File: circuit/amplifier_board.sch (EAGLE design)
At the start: 17 parts

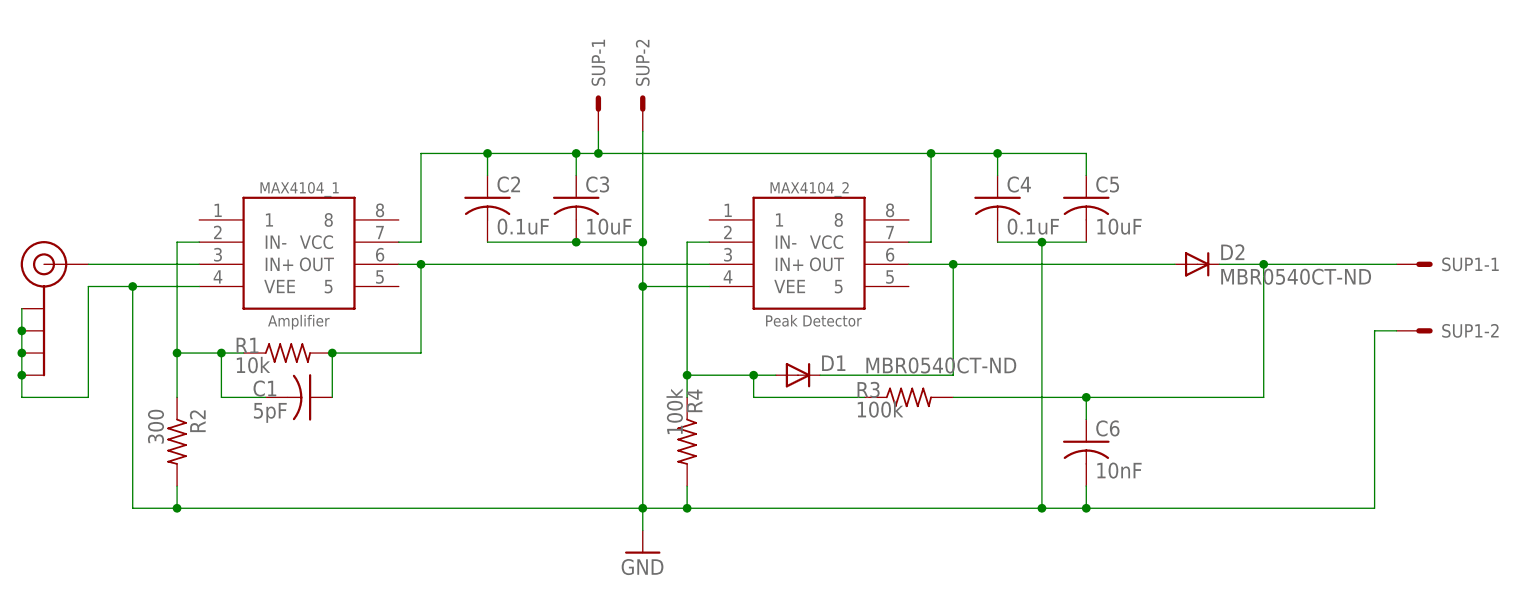
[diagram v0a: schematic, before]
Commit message: Modified board. Tried to add Spice model.
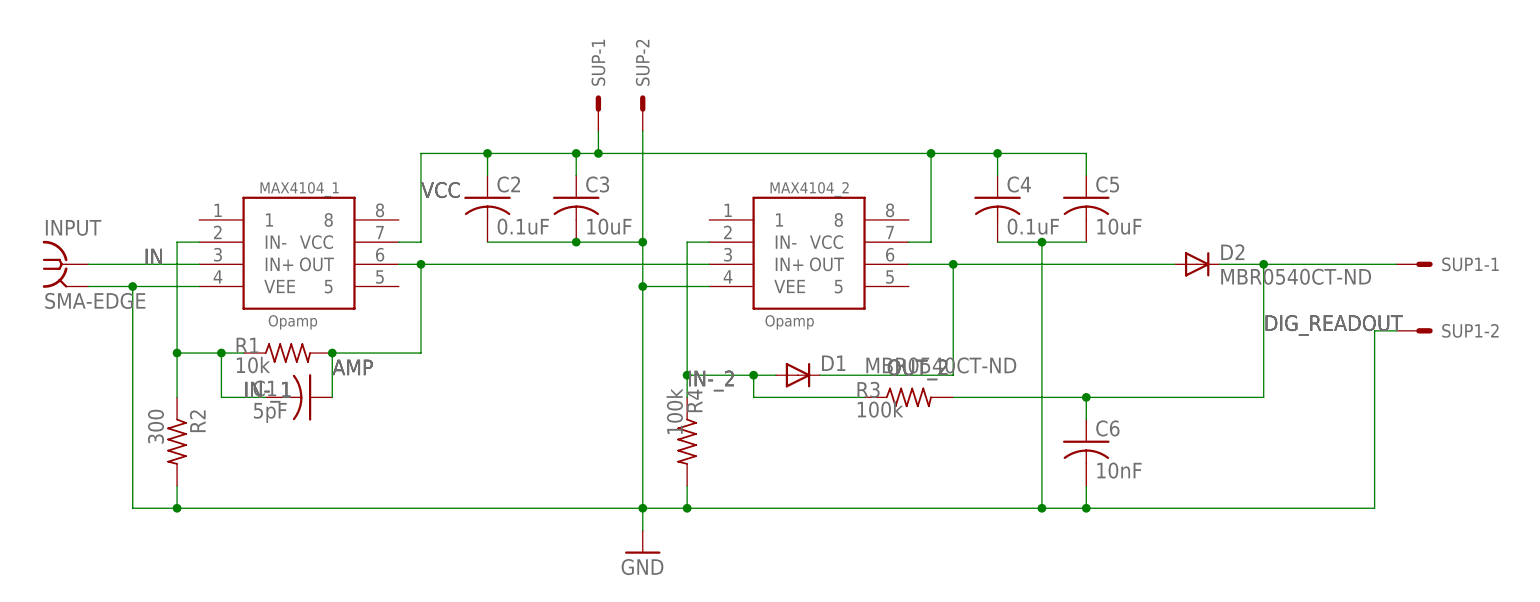
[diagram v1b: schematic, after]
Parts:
- removed IN: SMA_EDGE, SparkFun-Retired:SMA_EDGE
- added INPUT: SMA-EDGE, 000phys605parts:SMA-EDGE
- D1, D2: SPICEMODEL (none) -> DMBR0540; SPICEPREFIX (none) -> D
- MAX4104_1: value Amplifier -> Opamp; SPICEMODEL (none) -> MAX4104; SPICEPREFIX (none) -> X
- MAX4104_2: value Peak Detector -> Opamp; SPICEMODEL (none) -> MAX4104; SPICEPREFIX (none) -> X
- SUP: SPICEMODEL (none) -> VoltageSource; SPICEPREFIX (none) -> X
- SUP1: SPICEMODEL (none) -> TerminalOut; SPICEPREFIX (none) -> X
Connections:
- net GND: now also INPUT.2; no longer IN.GND@0, IN.GND@1, IN.GND@2, IN.GND@3
- net IN: now also INPUT.1; no longer IN.SIGNAL
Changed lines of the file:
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@@
 </classes>
 <parts>
-<part name="MAX4104_1" library="000phys605parts" deviceset="MAX4104" device="" value="Amplifier"/>
+<part name="MAX4104_1" library="000phys605parts" deviceset="MAX4104" device="" value="Opamp">
+<spice>
+<pinmapping isusermap="yes" isdevicewide="no">
+<pinmap gate="G$1" pin="1" pinorder="6"/>
+<pinmap gate="G$1" pin="5" pinorder="7"/>
+<pinmap gate="G$1" pin="8" pinorder="8"/>
+<pinmap gate="G$1" pin="IN+" pinorder="1"/>
+<pinmap gate="G$1" pin="IN-" pinorder="2"/>
+<pinmap gate="G$1" pin="OUT" pinorder="5"/>
+<pinmap gate="G$1" pin="VCC" pinorder="3"/>
+<pinmap gate="G$1" pin="VEE" pinorder="4"/>
+</pinmapping>
+</spice>
+<attribute name="SPICEMODEL" value="MAX4104"/>
+<attribute name="SPICEPREFIX" value="X"/>
+</part>
 <part name="R1" library="rcl" library_urn="urn:adsk.eagle:library:334" deviceset="R-US_" device="M0805" package3d_urn="urn:adsk.eagle:package:23556/1" value="10k"/>
 <part name="R2" library="rcl" library_urn="urn:adsk.eagle:library:334" deviceset="R-US_" device="M0805" package3d_urn="urn:adsk.eagle:package:23556/1" value="300"/>
@@
 <part name="C3" library="rcl" library_urn="urn:adsk.eagle:library:334" deviceset="C-US" device="C0805" package3d_urn="urn:adsk.eagle:package:23617/2" value="10uF"/>
 <part name="C2" library="rcl" library_urn="urn:adsk.eagle:library:334" deviceset="C-US" device="C0805" package3d_urn="urn:adsk.eagle:package:23617/2" value="0.1uF"/>
-<part name="SUP" library="con-garry" library_urn="urn:adsk.eagle:library:147" deviceset="332-02" device="" package3d_urn="urn:adsk.eagle:package:6810/1"/>
-<part name="MAX4104_2" library="000phys605parts" deviceset="MAX4104" device="" value="Peak Detector"/>
+<part name="SUP" library="con-garry" library_urn="urn:adsk.eagle:library:147" deviceset="332-02" device="" package3d_urn="urn:adsk.eagle:package:6810/1">
+<spice>
+<pinmapping isusermap="yes" isdevicewide="no">
+<pinmap gate="-1" pin="S" pinorder="1"/>
+<pinmap gate="-2" pin="S" pinorder="2"/>
+</pinmapping>
+</spice>
+<attribute name="SPICEMODEL" value="VoltageSource"/>
+<attribute name="SPICEPREFIX" value="X"/>
+</part>
+<part name="MAX4104_2" library="000phys605parts" deviceset="MAX4104" device="" value="Opamp">
+<spice>
+<pinmapping isusermap="yes" isdevicewide="no">
+<pinmap gate="G$1" pin="1" pinorder="6"/>
+<pinmap gate="G$1" pin="5" pinorder="7"/>
+<pinmap gate="G$1" pin="8" pinorder="8"/>
+<pinmap gate="G$1" pin="IN+" pinorder="1"/>
+<pinmap gate="G$1" pin="IN-" pinorder="2"/>
+<pinmap gate="G$1" pin="OUT" pinorder="5"/>
+<pinmap gate="G$1" pin="VCC" pinorder="3"/>
+<pinmap gate="G$1" pin="VEE" pinorder="4"/>
+</pinmapping>
+</spice>
+<attribute name="SPICEMODEL" value="MAX4104"/>
+<attribute name="SPICEPREFIX" value="X"/>
+</part>
 <part name="C4" library="rcl" library_urn="urn:adsk.eagle:library:334" deviceset="C-US" device="C0805" package3d_urn="urn:adsk.eagle:package:23617/2" value="0.1uF"/>
 <part name="C5" library="rcl" library_urn="urn:adsk.eagle:library:334" deviceset="C-US" device="C0805" package3d_urn="urn:adsk.eagle:package:23617/2" value="10uF"/>
-<part name="GND2" library="supply1" library_urn="urn:adsk.eagle:library:371" deviceset="GND" device=""/>
+<part name="GND2" library="supply1" library_urn="urn:adsk.eagle:library:371" deviceset="GND" device="">
+<attribute name="SPICEGROUND" value=""/>
+<attribute name="SPICEPREFIX" value="G"/>
+</part>
 <part name="R3" library="rcl" library_urn="urn:adsk.eagle:library:334" deviceset="R-US_" device="M0805" package3d_urn="urn:adsk.eagle:package:23556/1" value="100k"/>
 <part name="R4" library="rcl" library_urn="urn:adsk.eagle:library:334" deviceset="R-US_" device="M0805" package3d_urn="urn:adsk.eagle:package:23556/1" value="100k"/>
 <part name="C6" library="rcl" library_urn="urn:adsk.eagle:library:334" deviceset="C-US" device="C0805" package3d_urn="urn:adsk.eagle:package:23617/2" value="10nF"/>
-<part name="IN" library="SparkFun-Retired" deviceset="SMA_EDGE" device=""/>
-<part name="D1" library="diode" library_urn="urn:adsk.eagle:library:210" deviceset="CGRM400*-G" device="" package3d_urn="urn:adsk.eagle:package:43457/2" technology="1" value="MBR0540CT-ND"/>
-<part name="D2" library="diode" library_urn="urn:adsk.eagle:library:210" deviceset="CGRM400*-G" device="" package3d_urn="urn:adsk.eagle:package:43457/2" technology="1" value="MBR0540CT-ND"/>
-<part name="SUP1" library="con-garry" library_urn="urn:adsk.eagle:library:147" deviceset="332-02" device="" package3d_urn="urn:adsk.eagle:package:6810/1"/>
+<part name="D1" library="diode" library_urn="urn:adsk.eagle:library:210" deviceset="CGRM400*-G" device="" package3d_urn="urn:adsk.eagle:package:43457/2" technology="1" value="MBR0540CT-ND">
+<spice>
+<pinmapping isusermap="yes" isdevicewide="no">
+<pinmap gate="G$1" pin="A" pinorder="1"/>
+<pinmap gate="G$1" pin="C" pinorder="2"/>
+</pinmapping>
+</spice>
+<attribute name="SPICEMODEL" value="DMBR0540"/>
+<attribute name="SPICEPREFIX" value="D"/>
+</part>
+<part name="D2" library="diode" library_urn="urn:adsk.eagle:library:210" deviceset="CGRM400*-G" device="" package3d_urn="urn:adsk.eagle:package:43457/2" technology="1" value="MBR0540CT-ND">
+<spice>
+<pinmapping isusermap="yes" isdevicewide="no">
+<pinmap gate="G$1" pin="A" pinorder="1"/>
+<pinmap gate="G$1" pin="C" pinorder="2"/>
+</pinmapping>
+</spice>
+<attribute name="SPICEMODEL" value="DMBR0540"/>
+<attribute name="SPICEPREFIX" value="D"/>
+</part>
+<part name="SUP1" library="con-garry" library_urn="urn:adsk.eagle:library:147" deviceset="332-02" device="" package3d_urn="urn:adsk.eagle:package:6810/1">
+<spice>
+<pinmapping isusermap="yes" isdevicewide="no">
+<pinmap gate="-1" pin="S" pinorder="1"/>
+<pinmap gate="-2" pin="S" pinorder="2"/>
+</pinmapping>
+</spice>
+<attribute name="SPICEMODEL" value="TerminalOut"/>
+<attribute name="SPICEPREFIX" value="X"/>
+</part>
+<part name="INPUT" library="000phys605parts" deviceset="SMA-EDGE" device="">
+<spice>
+<pinmapping isusermap="yes" isdevicewide="yes">
+<pinmap gate="G$1" pin="1" pinorder="1"/>
+<pinmap gate="G$1" pin="2" pinorder="2"/>
+</pinmapping>
+</spice>
+<attribute name="SPICEPREFIX" value="V"/>
+</part>
 </parts>
 <sheets>
@@
 </instance>
 <instance part="C6" gate="G$1" x="160.02" y="30.48"/>
-<instance part="IN" gate="1" x="40.64" y="50.8"/>
 <instance part="D1" gate="G$1" x="127" y="38.1" smashed="yes">
 <attribute name="NAME" x="129.54" y="38.5826" size="1.778" layer="95"/>
@@
 <instance part="SUP1" gate="-2" x="198.12" y="43.18" smashed="yes">
 <attribute name="NAME" x="200.66" y="42.418" size="1.524" layer="95"/>
+</instance>
+<instance part="INPUT" gate="G$1" x="43.18" y="50.8">
+<label x="43.18" y="50.8" size="1.778" layer="88" ratio="9"/>
+<label x="43.18" y="50.8" size="1.778" layer="88" ratio="9"/>
 </instance>
 </instances>
@@
 <wire x1="83.82" y1="40.64" x2="83.82" y2="50.8" width="0.1524" layer="91"/>
 <junction x="83.82" y="50.8"/>
+<label x="73.66" y="38.1" size="1.778" layer="88" ratio="9"/>
+<label x="73.66" y="38.1" size="1.778" layer="88" ratio="9"/>
 </segment>
 </net>
@@
 <wire x1="55.88" y1="53.34" x2="55.88" y2="40.64" width="0.1524" layer="91"/>
 <junction x="55.88" y="40.64"/>
+<label x="63.5" y="35.56" size="1.778" layer="88" ratio="9"/>
+<label x="63.5" y="35.56" size="1.778" layer="88" ratio="9"/>
 </segment>
 </net>
@@
 <junction x="50.8" y="48.26"/>
 <junction x="160.02" y="22.86"/>
-<wire x1="45.72" y1="48.26" x2="45.72" y2="35.56" width="0.1524" layer="91"/>
-<wire x1="45.72" y1="35.56" x2="38.1" y2="35.56" width="0.1524" layer="91"/>
-<pinref part="IN" gate="1" pin="GND@3"/>
-<wire x1="38.1" y1="35.56" x2="38.1" y2="38.1" width="0.1524" layer="91"/>
-<pinref part="IN" gate="1" pin="GND@2"/>
-<wire x1="38.1" y1="38.1" x2="38.1" y2="40.64" width="0.1524" layer="91"/>
-<junction x="38.1" y="38.1"/>
-<pinref part="IN" gate="1" pin="GND@1"/>
-<wire x1="38.1" y1="40.64" x2="38.1" y2="43.18" width="0.1524" layer="91"/>
-<junction x="38.1" y="40.64"/>
-<pinref part="IN" gate="1" pin="GND@0"/>
-<wire x1="38.1" y1="43.18" x2="38.1" y2="45.72" width="0.1524" layer="91"/>
-<junction x="38.1" y="43.18"/>
 <wire x1="160.02" y1="22.86" x2="193.04" y2="22.86" width="0.1524" layer="91"/>
 <wire x1="193.04" y1="22.86" x2="193.04" y2="43.18" width="0.1524" layer="91"/>
 <pinref part="SUP1" gate="-2" pin="S"/>
 <wire x1="193.04" y1="43.18" x2="195.58" y2="43.18" width="0.1524" layer="91"/>
+<pinref part="INPUT" gate="G$1" pin="2"/>
 </segment>
 </net>
@@
 <wire x1="175.26" y1="50.8" x2="180.34" y2="50.8" width="0.1524" layer="91"/>
 <pinref part="SUP1" gate="-1" pin="S"/>
+<label x="180.34" y="43.18" size="1.778" layer="88" ratio="9"/>
+<label x="180.34" y="43.18" size="1.778" layer="88" ratio="9"/>
 </segment>
 </net>
@@
 <pinref part="D1" gate="G$1" pin="C"/>
 <pinref part="D2" gate="G$1" pin="A"/>
+<label x="137.16" y="38.1" size="1.778" layer="88" ratio="9"/>
+<label x="137.16" y="38.1" size="1.778" layer="88" ratio="9"/>
 </segment>
 </net>
@@
 <wire x1="121.92" y1="38.1" x2="124.46" y2="38.1" width="0.1524" layer="91"/>
 <junction x="121.92" y="38.1"/>
+<label x="114.3" y="36.83" size="1.778" layer="88" ratio="9"/>
+<label x="114.3" y="36.83" size="1.778" layer="88" ratio="9"/>
 </segment>
 </net>
@@
 <pinref part="C5" gate="G$1" pin="1"/>
 <wire x1="160.02" y1="63.5" x2="160.02" y2="60.96" width="0.1524" layer="91"/>
+<label x="83.82" y="58.42" size="1.778" layer="88" ratio="9"/>
+<label x="83.82" y="58.42" size="1.778" layer="88" ratio="9"/>
 </segment>
 </net>
@@
 <pinref part="MAX4104_1" gate="G$1" pin="IN+"/>
 <wire x1="58.42" y1="50.8" x2="45.72" y2="50.8" width="0.1524" layer="91"/>
-<pinref part="IN" gate="1" pin="SIGNAL"/>
-</segment>
-</net>
+<pinref part="INPUT" gate="G$1" pin="1"/>
+<label x="52.07" y="50.8" size="1.778" layer="88" ratio="9"/>
+<label x="52.07" y="50.8" size="1.778" layer="88" ratio="9"/>
+</segment>
+</net>
